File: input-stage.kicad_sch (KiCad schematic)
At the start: 20 parts, among them U7 AD8221ARZ, U8 Opamp_Dual

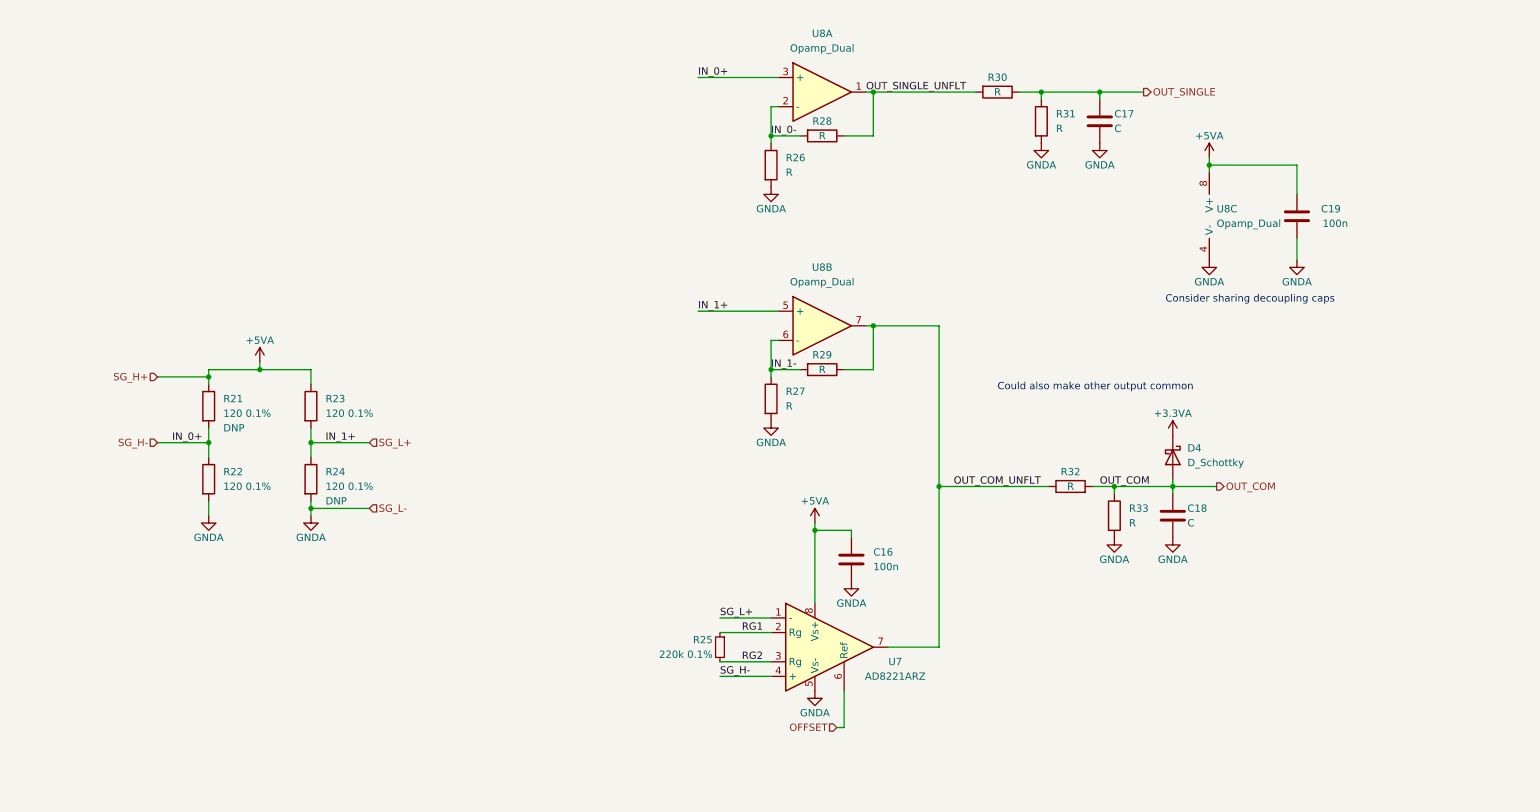
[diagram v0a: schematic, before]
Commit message: sch: add power delivery network and finalize schematic
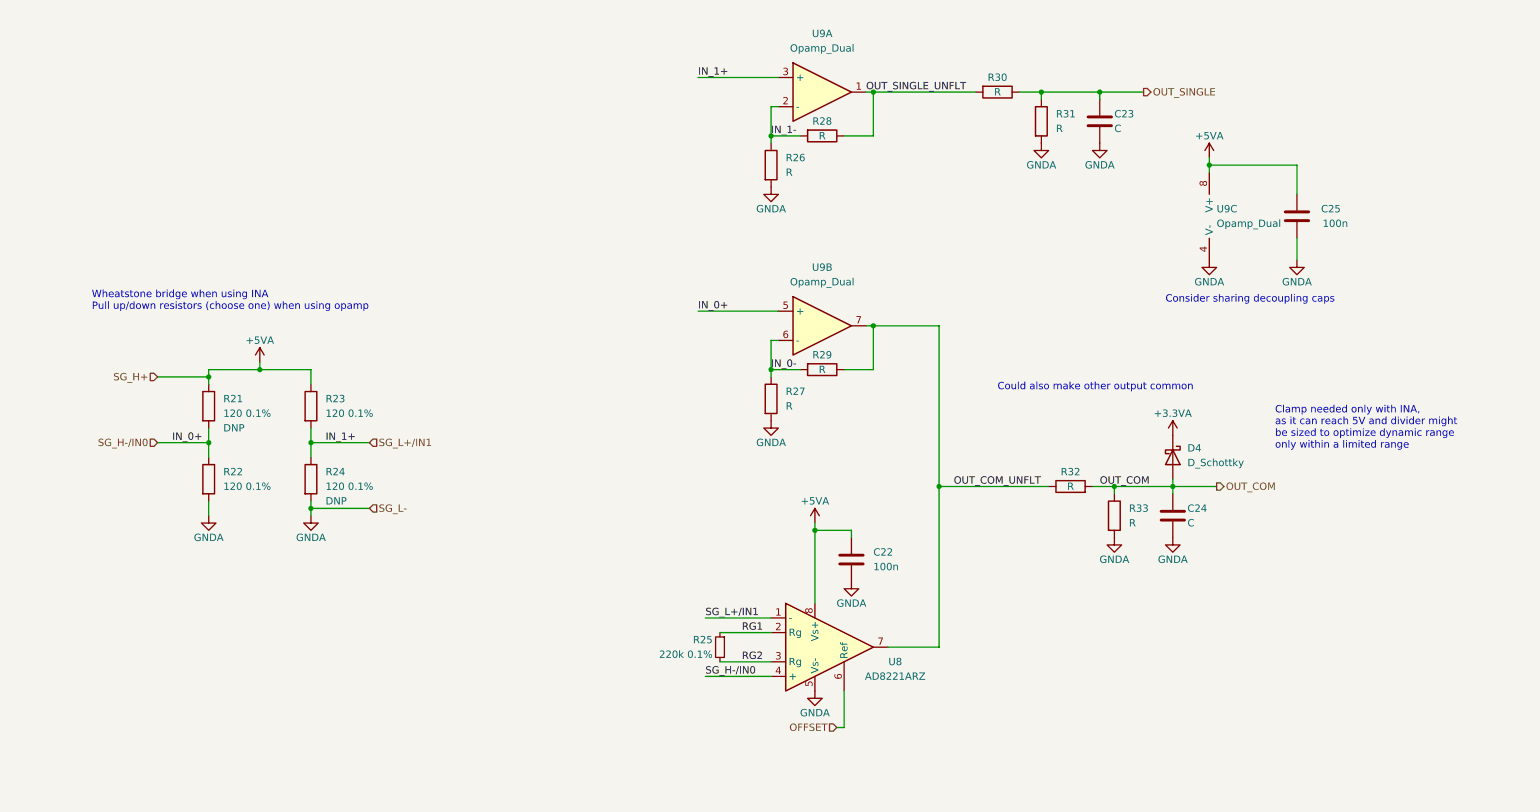
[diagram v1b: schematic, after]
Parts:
- C23: renamed from C17; footprint Capacitor_SMD:C_0603_1608Metric -> Capacitor_SMD:C_0805_2012Metric
- C24: renamed from C18; footprint Capacitor_SMD:C_0603_1608Metric -> Capacitor_SMD:C_0805_2012Metric
- D4: footprint Diode_SMD:D_SOD-523 -> Diode_SMD:D_SOD-123
- renumbered C16 to C22, C19 to C25, U7 to U8, U8 to U9
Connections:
- net IN_0-: now also R27.1, R29.2, U9.6 (-); no longer R26.1, R28.2, U9.2 (-)
- net IN_1-: now also R26.1, R28.2, U9.2 (-); no longer R27.1, R29.2, U9.6 (-)
- net SG_H- renamed SG_H-/IN0
- net SG_H-/IN0: now also U9.5 (+); no longer U9.3 (+)
- net SG_L+ renamed SG_L+/IN1
- net SG_L+/IN1: now also U9.3 (+); no longer U9.5 (+)
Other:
- note added: "Clamp needed only with INA, as it can reach 5V and divider might be sized to optimize dynamic range only within a limited range"
- note added: "Wheatstone bridge when using INA Pull up/down resistors (choose one) when using opamp"
- company: (none) -> E-Agle TRT
- title: (none) -> An2CAN

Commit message: sch: change single input connector to 4 02x02
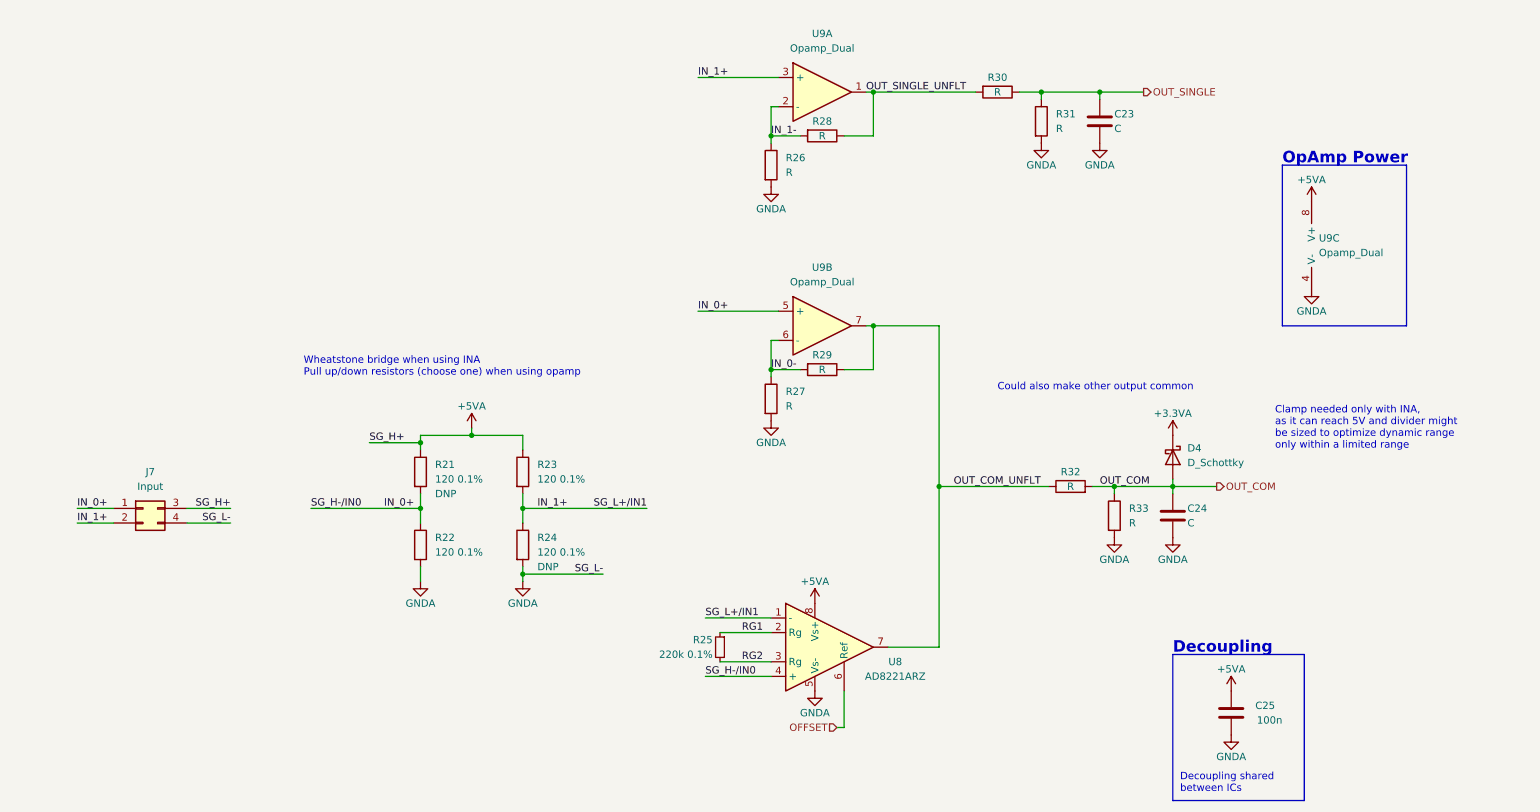
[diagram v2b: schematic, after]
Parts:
- removed C22: 100n, Capacitor_SMD:C_0603_1608Metric, symbol Device:C
- added J7: Input, Connector_Molex:Molex_Nano-Fit_105314-xx04_2x02_P2.50mm_Horizontal, symbol Connector_Generic:Conn_02x02_Top_Bottom
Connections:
- net +5VA: now also J7.3 (Pin_3)
- net GNDA: now also J7.4 (Pin_4)
- net SG_H-/IN0 renamed IN_0+
- net IN_0+: now also J7.1 (Pin_1)
- net SG_L+/IN1 renamed IN_1+
- net IN_1+: now also J7.2 (Pin_2)
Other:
- note added: "Decoupling"
- note added: "Decoupling shared between ICs"
- note added: "OpAmp Power"
- note removed: "Consider sharing decoupling caps"
- moved on the sheet: C25, R21, R22, R23, R24, U9C

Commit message: sch: add input series resistor to form divider and clamp to opamp output
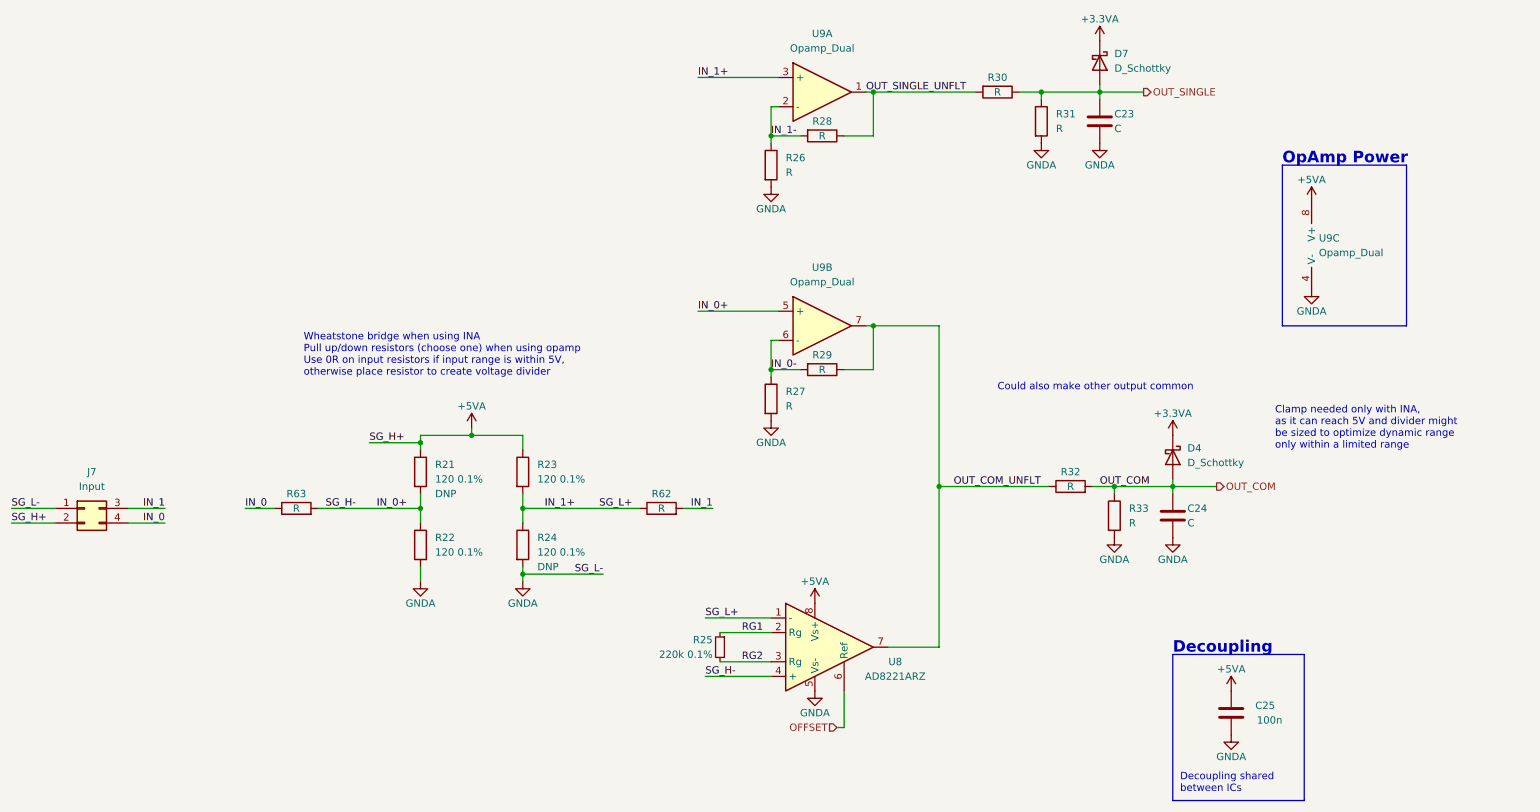
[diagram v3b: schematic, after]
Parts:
- added D7: D_Schottky, Diode_SMD:D_SOD-123, symbol Device:D_Schottky
- added R62, R63: R, Resistor_SMD:R_0603_1608Metric, symbol Device:R
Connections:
- net +3.3VA: now also D7.1 (K)
- net +5VA: now also J7.2 (Pin_2); no longer J7.3 (Pin_3)
- net GNDA: now also J7.1 (Pin_1); no longer J7.4 (Pin_4)
- net IN_0+: now also R63.2; no longer J7.1 (Pin_1)
- net IN_1+: now also R62.1; no longer J7.2 (Pin_2)
- net OUT_SINGLE: now also D7.2 (A)
- new net IN_0: J7.4 (Pin_4), R63.1
- new net IN_1: J7.3 (Pin_3), R62.2
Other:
- note added: "Wheatstone bridge when using INA Pull up/down resistors (choose one) when using opamp Use 0R on input resistors if input range is within 5V, otherwise place resistor to create voltage divider"
- note removed: "Wheatstone bridge when using INA Pull up/down resistors (choose one) when using opamp"
- moved on the sheet: J7

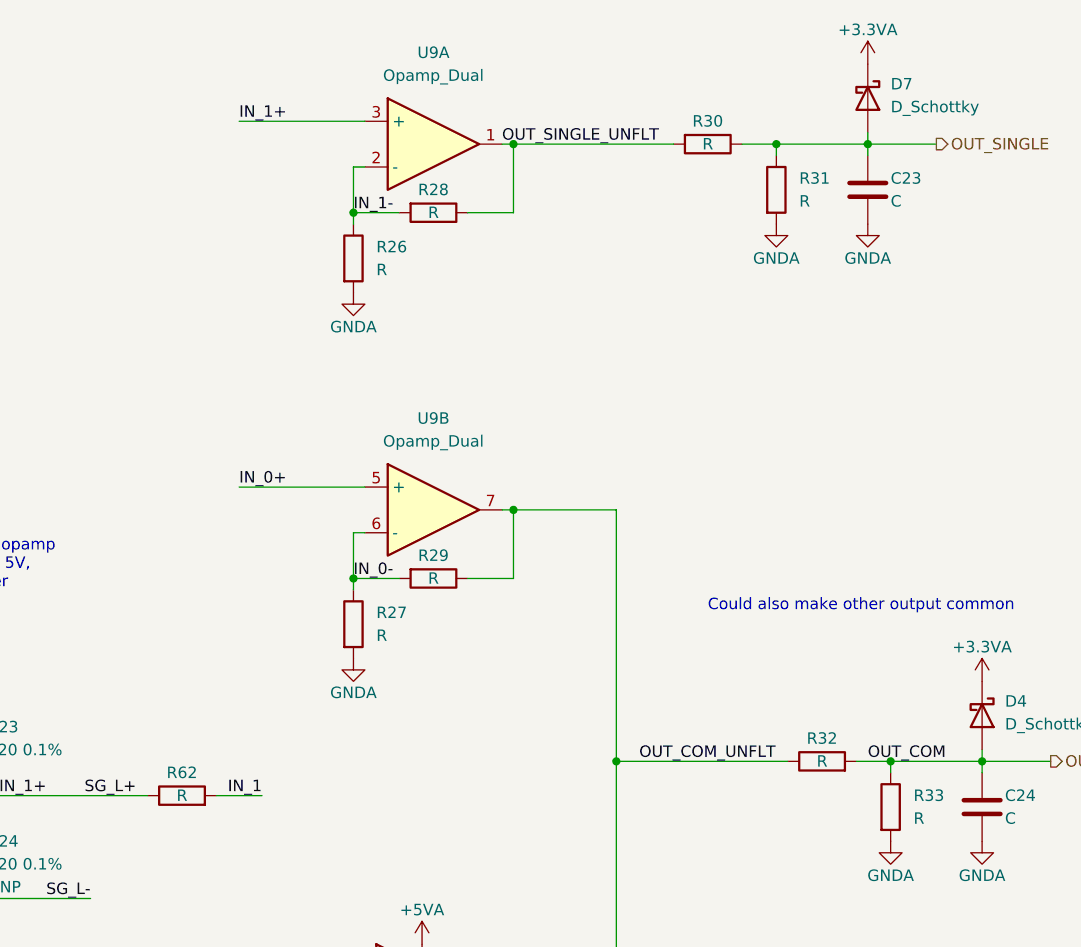
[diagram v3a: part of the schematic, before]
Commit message: pcb: finalize routing of analog section
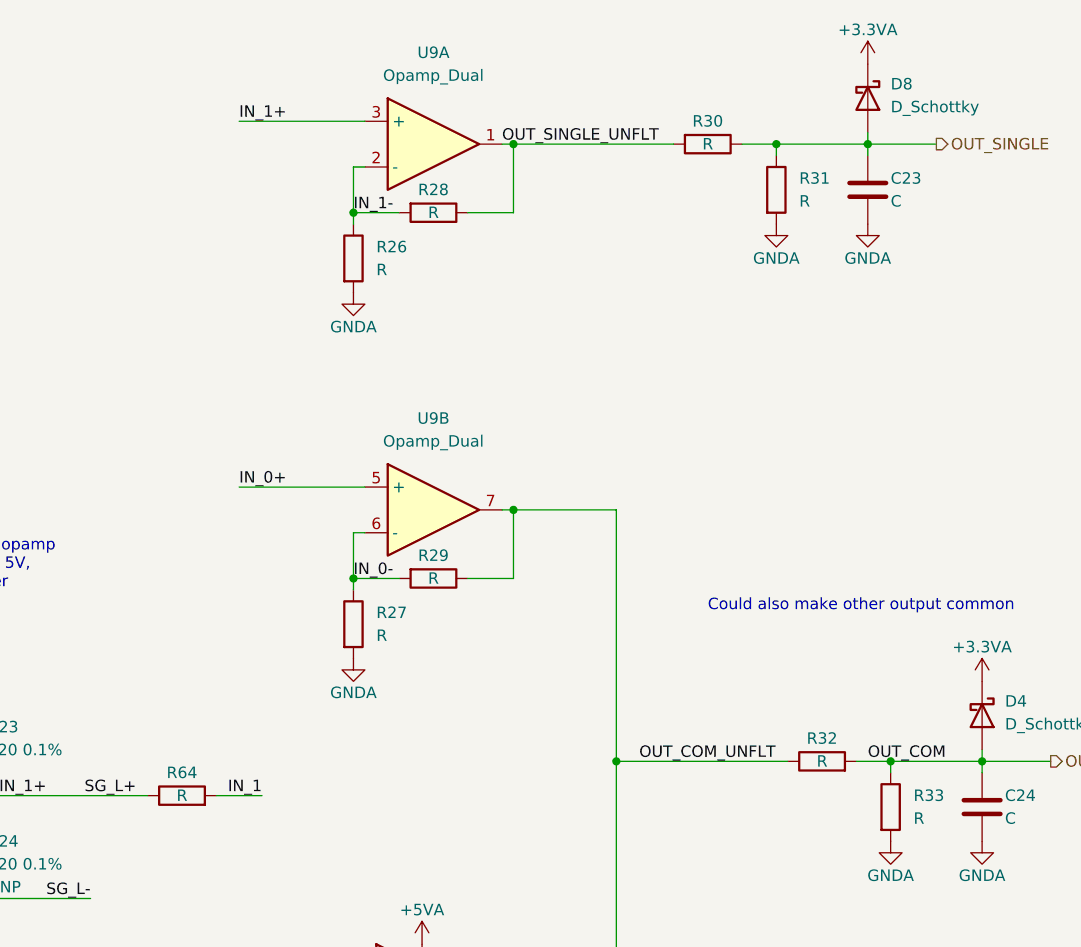
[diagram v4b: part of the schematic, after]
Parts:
- renumbered D7 to D8, R62 to R64
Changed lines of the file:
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@@
   (symbol (lib_id "Device:R") (at 137.16 101.6 90) (unit 1)
     (in_bom yes) (on_board yes)
-    (property "Reference" "R62" (id 0) (at 137.16 99.06 90))
+    (property "Reference" "R64" (id 0) (at 137.16 99.06 90))
     (property "Value" "R" (id 1) (at 137.16 101.6 90))
     (property "Footprint" "Resistor_SMD:R_0603_1608Metric" (id 2) (at 137.16 103.378 90)
@@
   (symbol (lib_id "power:+3.3VA") (at 213.36 20.32 0) (unit 1)
     (in_bom yes) (on_board yes)
-    (property "Reference" "#PWR0134" (id 0) (at 213.36 24.13 0)
+    (property "Reference" "#PWR0135" (id 0) (at 213.36 24.13 0)
       (effects (font (size 1.27 1.27)) hide)
     )
@@
   (symbol (lib_id "Device:D_Schottky") (at 213.36 24.13 270) (unit 1)
     (in_bom yes) (on_board yes) (fields_autoplaced)
-    (property "Reference" "D7" (id 0) (at 215.9 22.5424 90)
-      (effects (font (size 1.27 1.27)) (justify left))
-    )
+    (property "Reference" "D8" (id 0) (at 215.9 22.5424 90)
+      (effects (font (size 1.27 1.27)) (justify left))
+    )
